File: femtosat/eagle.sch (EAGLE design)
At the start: 3 parts, among them U1 ATMEGA328P_TQFP, U2 915MHz

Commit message: Added Connecter
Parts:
- added J1: (no value), femtosat:CONNECTOR_6PINSILK_FEMALE_PTH
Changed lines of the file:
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@@
 <setting verticaltext="up"/>
 </settings>
-<grid distance="0.1" unitdist="inch" unit="inch" style="lines" multiple="1" display="yes" altdistance="0.01" altunitdist="inch" altunit="inch"/>
+<grid distance="0.1" unitdist="inch" unit="inch" style="lines" multiple="1" display="no" altdistance="0.01" altunitdist="inch" altunit="inch"/>
 <layers>
 <layer number="1" name="Top" color="4" fill="1" visible="no" active="no"/>
@@
 <part name="GND2" library="femtosat" deviceset="GND" device=""/>
 <part name="P+2" library="femtosat" deviceset="3.3V" device=""/>
+<part name="J1" library="femtosat" deviceset="CONNECTOR_6PIN" device="SILK_FEMALE_PTH"/>
 </parts>
 <sheets>
@@
 <attribute name="VALUE" x="92.964" y="150.876" size="1.778" layer="96"/>
 </instance>
+<instance part="J1" gate="G$1" x="48.26" y="116.84" smashed="yes">
+<attribute name="VALUE" x="43.18" y="106.68" size="1.778" layer="96"/>
+<attribute name="NAME" x="43.18" y="127.762" size="1.778" layer="95"/>
+</instance>
 </instances>

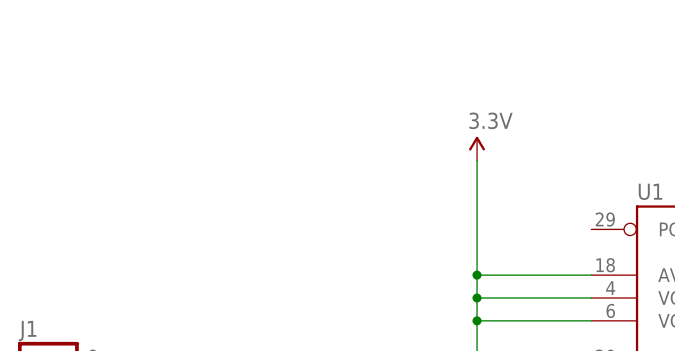
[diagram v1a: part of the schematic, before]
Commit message: Added 2pin connector
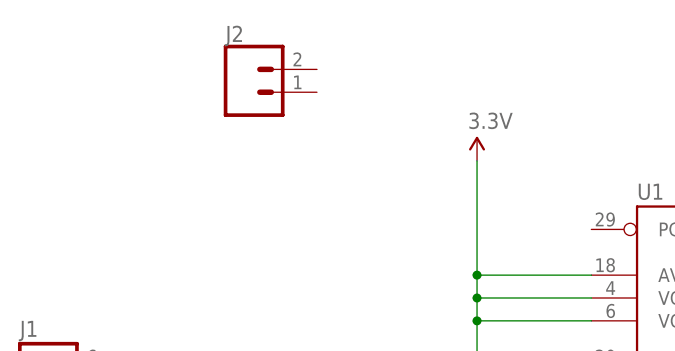
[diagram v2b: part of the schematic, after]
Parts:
- added J2: (no value), femtosat:CONNECTOR_2PIN
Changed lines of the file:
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@@
 <part name="P+2" library="femtosat" deviceset="3.3V" device=""/>
 <part name="J1" library="femtosat" deviceset="CONNECTOR_6PIN" device="SILK_FEMALE_PTH"/>
+<part name="J2" library="femtosat" deviceset="CONNECTOR_2PIN" device=""/>
 </parts>
 <sheets>
@@
 <attribute name="NAME" x="43.18" y="127.762" size="1.778" layer="95"/>
 </instance>
+<instance part="J2" gate="G$1" x="68.58" y="154.94" smashed="yes">
+<attribute name="VALUE" x="66.04" y="150.114" size="1.778" layer="96" font="vector"/>
+<attribute name="NAME" x="66.04" y="160.528" size="1.778" layer="95" font="vector"/>
+</instance>
 </instances>
